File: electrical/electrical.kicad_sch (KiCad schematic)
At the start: 0 parts

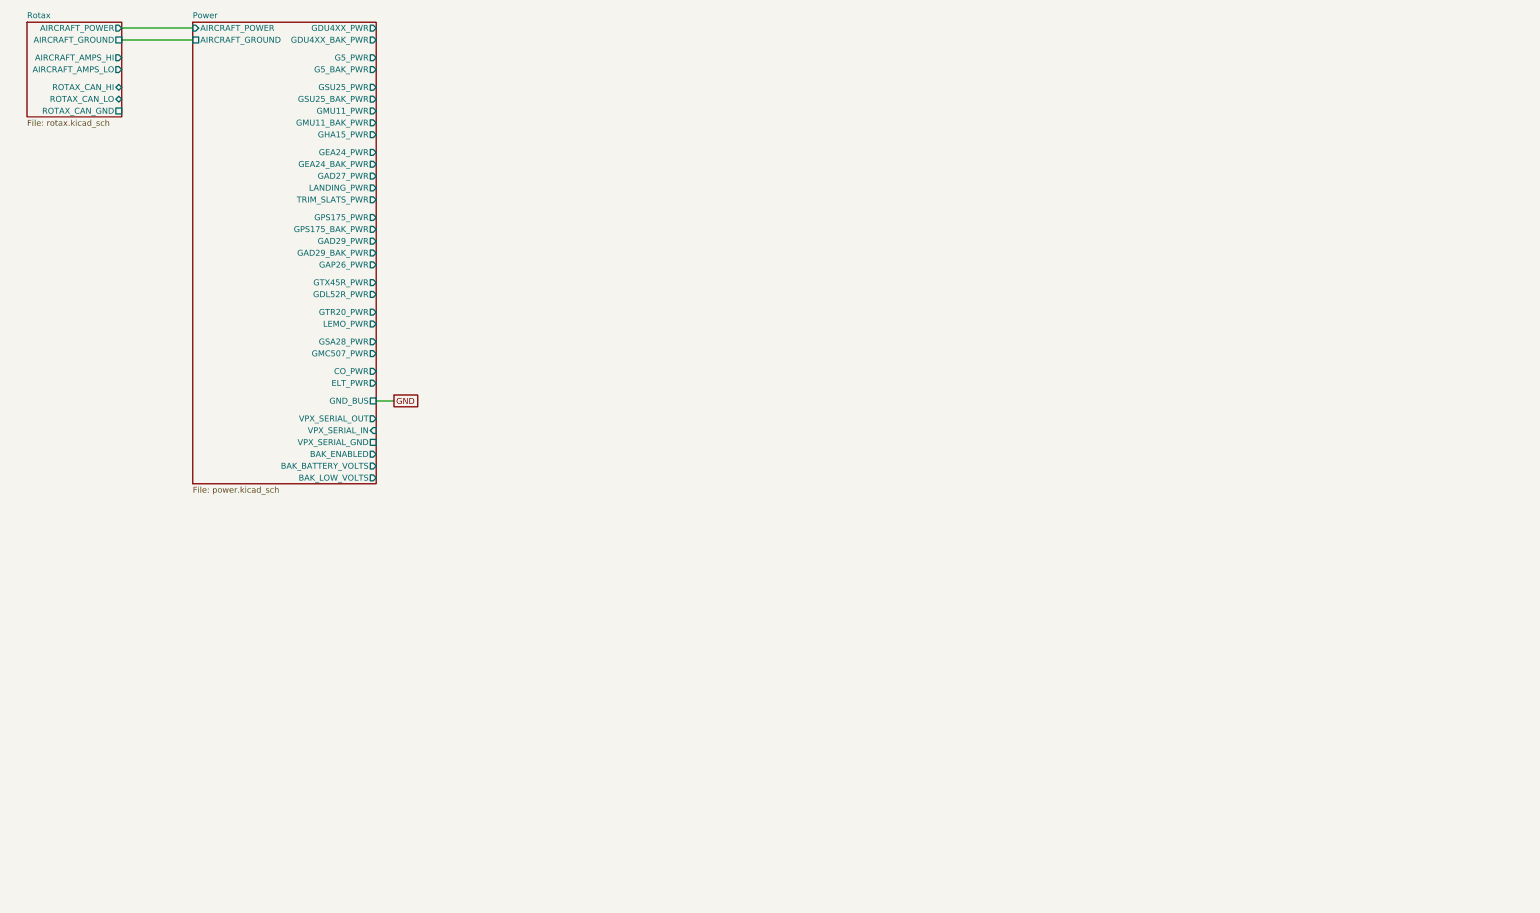
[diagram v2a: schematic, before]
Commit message: Added PFD and AirData
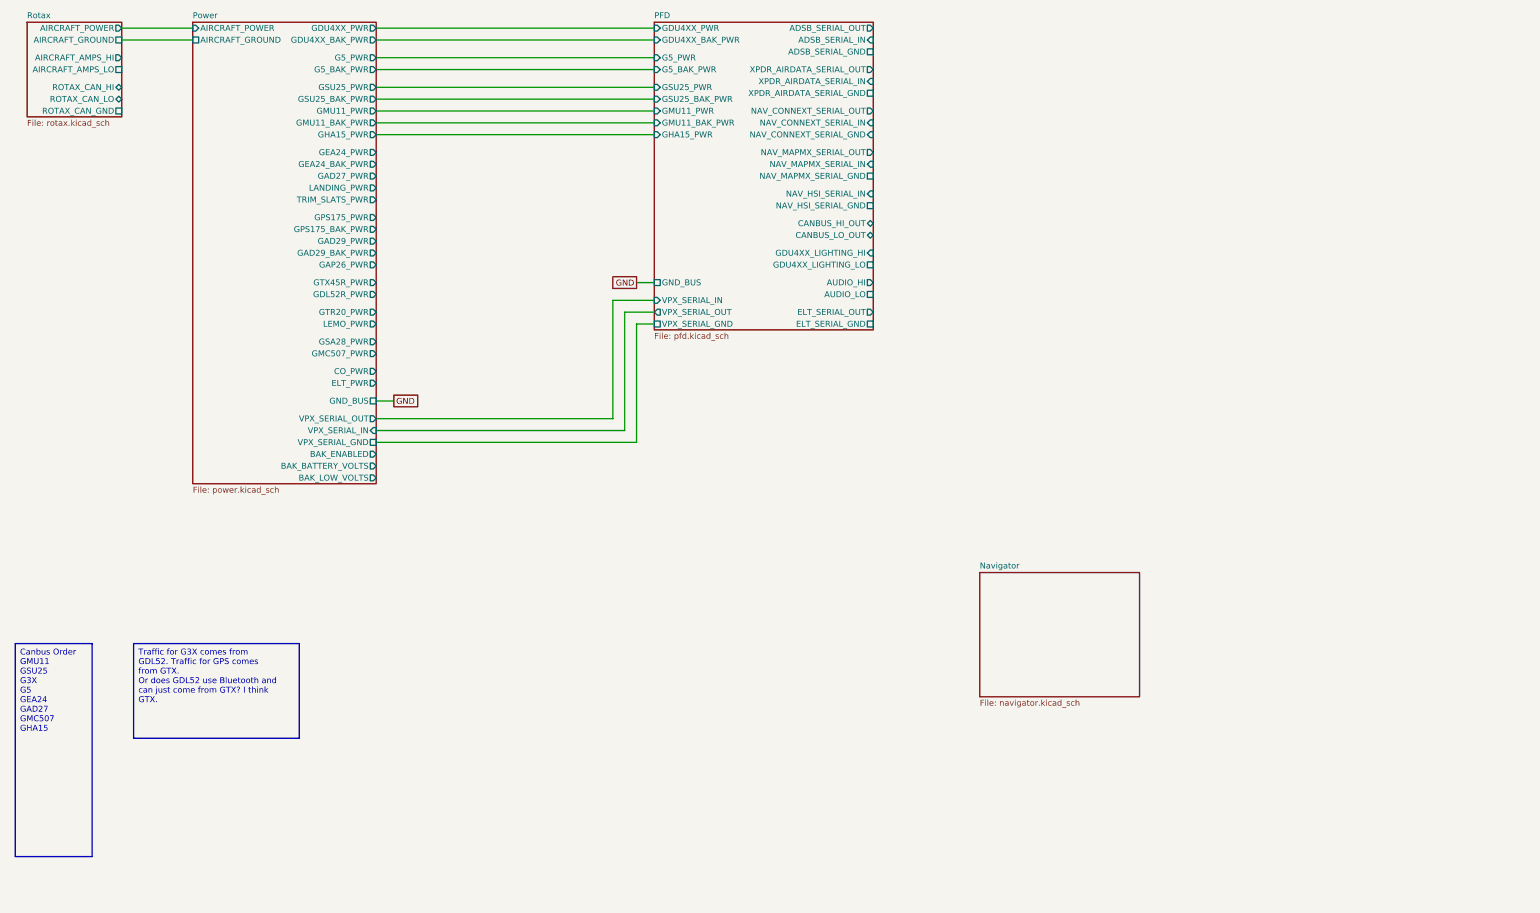
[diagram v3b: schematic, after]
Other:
- added sheet Navigator (navigator.kicad_sch)
- added sheet PFD (pfd.kicad_sch)
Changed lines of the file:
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@@
+    (stroke (width 0) (type default))
+  )
+  (wire (pts (xy 93.98 43.18) (xy 153.67 43.18))
+    (stroke (width 0) (type default))
+  )
+  (wire (pts (xy 93.98 40.64) (xy 153.67 40.64))
+    (stroke (width 0) (type default))
+  )
+  (wire (pts (xy 93.98 20.32) (xy 153.67 20.32))
+    (stroke (width 0) (type default))
+  )
+  (wire (pts (xy 93.98 38.1) (xy 153.67 38.1))
+    (stroke (width 0) (type default))
+  )
+  (wire (pts (xy 93.98 33.02) (xy 153.67 33.02))
+    (stroke (width 0) (type default))
+  )
+  (wire (pts (xy 93.98 104.14) (xy 144.78 104.14))
+    (stroke (width 0) (type default))
+  )
+  (wire (pts (xy 144.78 78.74) (xy 153.67 78.74))
+    (stroke (width 0) (type default))
+  )
+  (wire (pts (xy 93.98 106.68) (xy 147.32 106.68))
+    (stroke (width 0) (type default))
+  )
+  (wire (pts (xy 93.98 109.22) (xy 149.86 109.22))
+    (stroke (width 0) (type default))
+  )
+  (wire (pts (xy 147.32 81.28) (xy 153.67 81.28))
     (stroke (width 0) (type default))
   )
@@
     (stroke (width 0) (type default))
   )
+  (wire (pts (xy 93.98 26.67) (xy 153.67 26.67))
+    (stroke (width 0) (type default))
+  )
+  (wire (pts (xy 147.32 106.68) (xy 147.32 81.28))
+    (stroke (width 0) (type default))
+  )
+  (wire (pts (xy 93.98 35.56) (xy 153.67 35.56))
+    (stroke (width 0) (type default))
+  )
+  (wire (pts (xy 93.98 29.21) (xy 153.67 29.21))
+    (stroke (width 0) (type default))
+  )
+  (wire (pts (xy 93.98 22.86) (xy 153.67 22.86))
+    (stroke (width 0) (type default))
+  )
+  (wire (pts (xy 149.86 83.82) (xy 153.67 83.82))
+    (stroke (width 0) (type default))
+  )
+  (wire (pts (xy 144.78 104.14) (xy 144.78 78.74))
+    (stroke (width 0) (type default))
+  )
   (wire (pts (xy 39.37 20.32) (xy 54.61 20.32))
     (stroke (width 0) (type default))
+  )
+  (wire (pts (xy 149.86 74.93) (xy 153.67 74.93))
+    (stroke (width 0) (type default))
+  )
+  (wire (pts (xy 149.86 109.22) (xy 149.86 83.82))
+    (stroke (width 0) (type default))
+  )
+  (text_box "Traffic for G3X comes from GDL52. Traffic for GPS comes from GTX.\nOr does GDL52 use Bluetooth and can just come from GTX? I think GTX."
+    (at 41.91 152.4 0) (size 35.56 20.32)
+    (stroke (width 0) (type default))
+    (fill (type none))
+    (effects (font (size 1.27 1.27)) (justify left top))
+  )
+  (text_box "Canbus Order\nGMU11\nGSU25\nG3X\nG5\nGEA24\nGAD27\nGMC507\nGHA15\n"
+    (at 16.51 152.4 0) (size 16.51 45.72)
+    (stroke (width 0) (type default))
+    (fill (type none))
+    (effects (font (size 1.27 1.27)) (justify left top))
   )
   (global_label "GND" (shape passive) (at 97.79 100.33 0) (fields_autoplaced)
@@
     (property "Intersheetrefs" "${INTERSHEET_REFS}" (at 103.5344 100.33 0)
       (effects (font (size 1.27 1.27)) (justify left) hide)
+    )
+  )
+  (global_label "GND" (shape passive) (at 149.86 74.93 180) (fields_autoplaced)
+    (effects (font (size 1.27 1.27)) (justify right))
+    (property "Intersheetrefs" "${INTERSHEET_REFS}" (at 144.1156 74.93 0)
+      (effects (font (size 1.27 1.27)) (justify right) hide)
     )
   )
@@
       (effects (font (size 1.27 1.27)) (justify right))
     )
-    (pin "AIRCRAFT_AMPS_LO" output (at 39.37 29.21 0)
+    (pin "AIRCRAFT_AMPS_LO" passive (at 39.37 29.21 0)
       (effects (font (size 1.27 1.27)) (justify right))
     )
@@
       )
     )
+  )
+  (sheet (at 153.67 19.05) (size 46.99 66.04) (fields_autoplaced)
+    (stroke (width 0.1524) (type solid))
+    (fill (color 0 0 0 0.0000))
+    (property "Sheetname" "PFD" (at 153.67 18.3384 0)
+      (effects (font (size 1.27 1.27)) (justify left bottom))
+    )
+    (property "Sheetfile" "pfd.kicad_sch" (at 153.67 85.6746 0)
+      (effects (font (size 1.27 1.27)) (justify left top))
+    )
+    (pin "GND_BUS" passive (at 153.67 74.93 180)
+      (effects (font (size 1.27 1.27)) (justify left))
+    )
+    (pin "GDU4XX_LIGHTING_LO" passive (at 200.66 71.12 0)
+      (effects (font (size 1.27 1.27)) (justify right))
+    )
+    (pin "CANBUS_LO_OUT" bidirectional (at 200.66 64.77 0)
+      (effects (font (size 1.27 1.27)) (justify right))
+    )
+    (pin "CANBUS_HI_OUT" bidirectional (at 200.66 62.23 0)
+      (effects (font (size 1.27 1.27)) (justify right))
+    )
+    (pin "GDU4XX_LIGHTING_HI" input (at 200.66 68.58 0)
+      (effects (font (size 1.27 1.27)) (justify right))
+    )
+    (pin "GDU4XX_BAK_PWR" input (at 153.67 22.86 180)
+      (effects (font (size 1.27 1.27)) (justify left))
+    )
+    (pin "GDU4XX_PWR" input (at 153.67 20.32 180)
+      (effects (font (size 1.27 1.27)) (justify left))
+    )
+    (pin "GSU25_PWR" input (at 153.67 33.02 180)
+      (effects (font (size 1.27 1.27)) (justify left))
+    )
+    (pin "XPDR_AIRDATA_SERIAL_GND" passive (at 200.66 34.29 0)
+      (effects (font (size 1.27 1.27)) (justify right))
+    )
+    (pin "XPDR_AIRDATA_SERIAL_IN" input (at 200.66 31.75 0)
+      (effects (font (size 1.27 1.27)) (justify right))
+    )
+    (pin "GMU11_BAK_PWR" input (at 153.67 40.64 180)
+      (effects (font (size 1.27 1.27)) (justify left))
+    )
+    (pin "GMU11_PWR" input (at 153.67 38.1 180)
+      (effects (font (size 1.27 1.27)) (justify left))
+    )
+    (pin "GSU25_BAK_PWR" input (at 153.67 35.56 180)
+      (effects (font (size 1.27 1.27)) (justify left))
+    )
+    (pin "XPDR_AIRDATA_SERIAL_OUT" output (at 200.66 29.21 0)
+      (effects (font (size 1.27 1.27)) (justify right))
+    )
+    (pin "ADSB_SERIAL_OUT" output (at 200.66 20.32 0)
+      (effects (font (size 1.27 1.27)) (justify right))
+    )
+    (pin "ADSB_SERIAL_IN" input (at 200.66 22.86 0)
+      (effects (font (size 1.27 1.27)) (justify right))
+    )
+    (pin "NAV_MAPMX_SERIAL_OUT" output (at 200.66 46.99 0)
+      (effects (font (size 1.27 1.27)) (justify right))
+    )
+    (pin "ADSB_SERIAL_GND" passive (at 200.66 25.4 0)
+      (effects (font (size 1.27 1.27)) (justify right))
+    )
+    (pin "NAV_MAPMX_SERIAL_IN" input (at 200.66 49.53 0)
+      (effects (font (size 1.27 1.27)) (justify right))
+    )
+    (pin "NAV_HSI_SERIAL_GND" passive (at 200.66 58.42 0)
+      (effects (font (size 1.27 1.27)) (justify right))
+    )
+    (pin "NAV_CONNEXT_SERIAL_IN" input (at 200.66 40.64 0)
+      (effects (font (size 1.27 1.27)) (justify right))
+    )
+    (pin "VPX_SERIAL_GND" passive (at 153.67 83.82 180)
+      (effects (font (size 1.27 1.27)) (justify left))
+    )
+    (pin "NAV_CONNEXT_SERIAL_GND" input (at 200.66 43.18 0)
+      (effects (font (size 1.27 1.27)) (justify right))
+    )
+    (pin "VPX_SERIAL_OUT" output (at 153.67 81.28 180)
+      (effects (font (size 1.27 1.27)) (justify left))
+    )
+    (pin "VPX_SERIAL_IN" input (at 153.67 78.74 180)
+      (effects (font (size 1.27 1.27)) (justify left))
+    )
+    (pin "NAV_MAPMX_SERIAL_GND" passive (at 200.66 52.07 0)
+      (effects (font (size 1.27 1.27)) (justify right))
+    )
+    (pin "NAV_CONNEXT_SERIAL_OUT" output (at 200.66 38.1 0)
+      (effects (font (size 1.27 1.27)) (justify right))
+    )
+    (pin "AUDIO_LO" passive (at 200.66 77.47 0)
+      (effects (font (size 1.27 1.27)) (justify right))
+    )
+    (pin "AUDIO_HI" output (at 200.66 74.93 0)
+      (effects (font (size 1.27 1.27)) (justify right))
+    )
+    (pin "ELT_SERIAL_OUT" output (at 200.66 81.28 0)
+      (effects (font (size 1.27 1.27)) (justify right))
+    )
+    (pin "ELT_SERIAL_GND" passive (at 200.66 83.82 0)
+      (effects (font (size 1.27 1.27)) (justify right))
+    )
+    (pin "NAV_HSI_SERIAL_IN" input (at 200.66 55.88 0)
+      (effects (font (size 1.27 1.27)) (justify right))
+    )
+    (pin "G5_BAK_PWR" input (at 153.67 29.21 180)
+      (effects (font (size 1.27 1.27)) (justify left))
+    )
+    (pin "G5_PWR" input (at 153.67 26.67 180)
+      (effects (font (size 1.27 1.27)) (justify left))
+    )
+    (pin "GHA15_PWR" input (at 153.67 43.18 180)
+      (effects (font (size 1.27 1.27)) (justify left))
+    )
+    (instances
+      (project "electrical"
+        (path "/e8ec215a-dbe2-4eba-a577-e50a0a128049" (page "4"))
+      )
+    )
+  )
+  (sheet (at 223.52 137.16) (size 34.29 26.67) (fields_autoplaced)
+    (stroke (width 0.1524) (type solid))
+    (fill (color 0 0 0 0.0000))
+    (property "Sheetname" "Navigator" (at 223.52 136.4484 0)
+      (effects (font (size 1.27 1.27)) (justify left bottom))
+    )
+    (property "Sheetfile" "navigator.kicad_sch" (at 223.52 164.4146 0)
+      (effects (font (size 1.27 1.27)) (justify left top))
+    )
+    (instances
+      (project "electrical"
+        (path "/e8ec215a-dbe2-4eba-a577-e50a0a128049" (page "5"))
+      )
+    )

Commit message: Added Transponder and Navigator
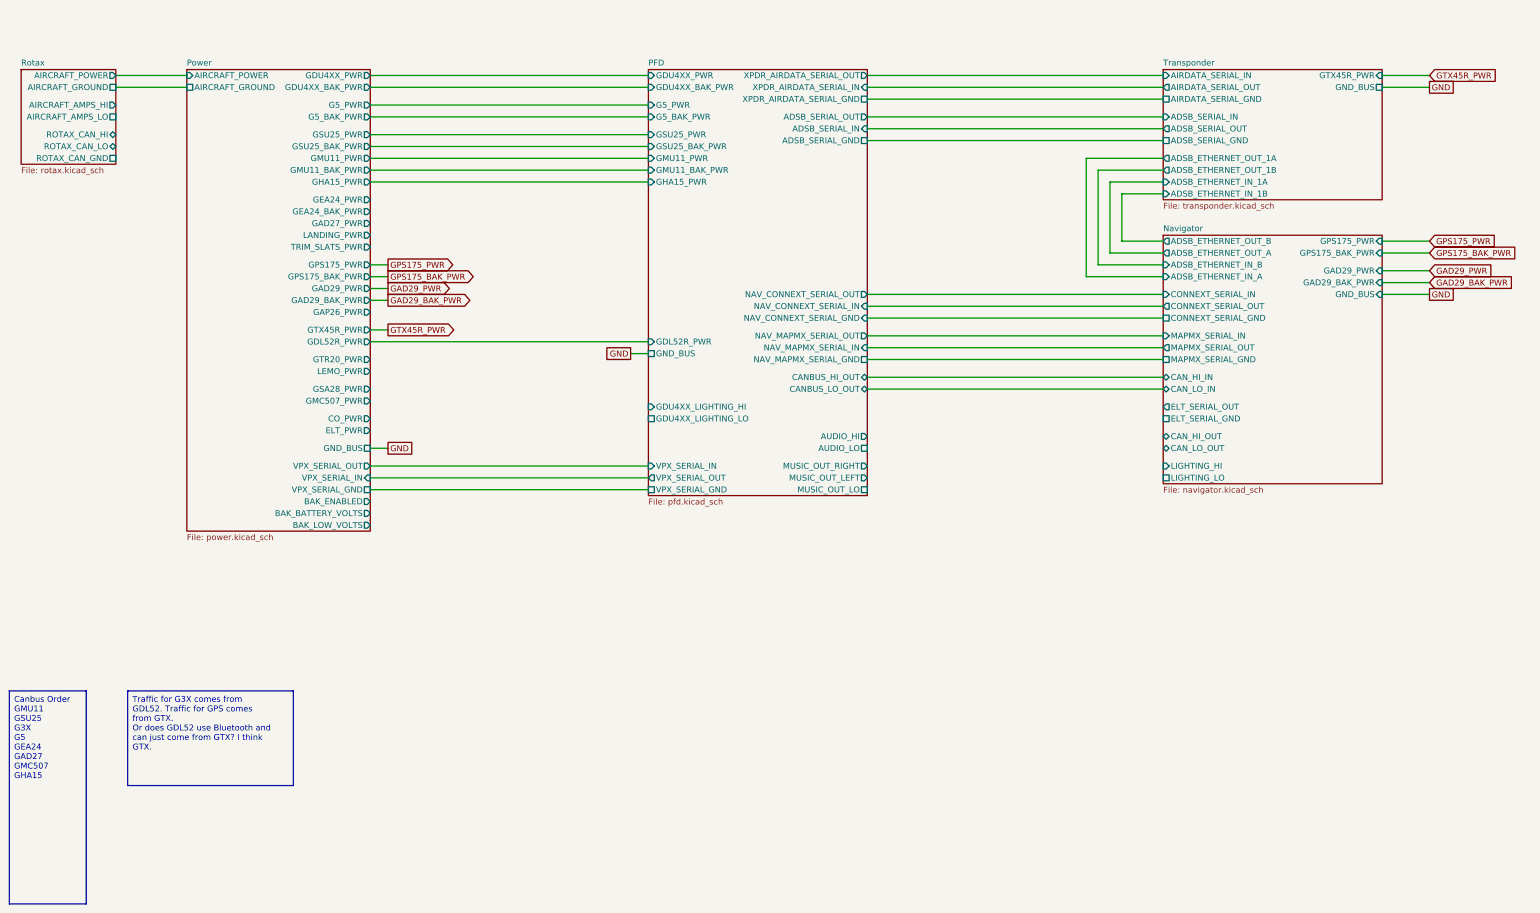
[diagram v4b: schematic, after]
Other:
- added sheet Transponder (transponder.kicad_sch)
- sheet Navigator ports: added ADSB_ETHERNET_IN_A, ADSB_ETHERNET_IN_B, ADSB_ETHERNET_OUT_A, ADSB_ETHERNET_OUT_B, CAN_HI_IN, CAN_HI_OUT, CAN_LO_IN, CAN_LO_OUT, CONNEXT_SERIAL_GND, CONNEXT_SERIAL_IN, CONNEXT_SERIAL_OUT, ELT_SERIAL_GND, ELT_SERIAL_OUT, GAD29_BAK_PWR, GAD29_PWR, GND_BUS, GPS175_BAK_PWR, GPS175_PWR, LIGHTING_HI, LIGHTING_LO, MAPMX_SERIAL_GND, MAPMX_SERIAL_IN, MAPMX_SERIAL_OUT; removed none
- sheet PFD ports: added GDL52R_PWR, MUSIC_OUT_LEFT, MUSIC_OUT_LO, MUSIC_OUT_RIGHT; removed ELT_SERIAL_GND, ELT_SERIAL_OUT, NAV_HSI_SERIAL_GND, NAV_HSI_SERIAL_IN
